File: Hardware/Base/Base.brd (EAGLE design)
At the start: 100 x 80 mm, 61 parts, among them IC1 LM2937, T1 2N3904, T10 2N3904, T2 2N3904, T3 2N3904, T4 2N3904, T5 2N3904, T6 2N3904, T7 2N3904, T8 2N3904, T9 2N3904

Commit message: Lay out components of base PCB rev0.
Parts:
- removed C1, C2: .01uF, rcl:C025-025X050
- removed IC1: LM2937, linear:TO263-3
- removed R4, R5, R6, R7: 10k, rcl:0207/7
- removed ROT-ENC: (no value), con-lstb:MA03-1
- removed TIVA1: TIVA-BOARD, tiva-board:TIVA-BOARD
- added C7, C8, C9: .01uF, rcl:C025-025X050
- added LEDGPIOC7: (no value), led:LED5MM
- added R25, R26: (no value), rcl:0207/7
- added R27, R28, R29, R30, R31, R32: 10k, rcl:0207/7
- added REG3V3: 7806T, linear:TO220H
- added ROTENC: (no value), con-lstb:MA05-1
- added SWITCH: (no value), pinhead:1X02
- added T11: 2N3904, transistor:TO92
- added TIVA: TIVA-BOARD, tiva-board:TIVA-BOARD
- X1: device con-yamaichi:USB-A003 -> con-berg:PN87520
- moved SERVO0 218.0 mm to (116.8, 76.2)
- moved LEDM1PWM3 217.2 mm to (115.6, 95.2)
- moved C4 187.6 mm to (110.5, 40.6), turned to 90 degrees
- moved T9 182.6 mm to (88.9, 90.2), turned to 180 degrees
- moved C3 179.1 mm to (120.7, 40.6), turned to 90 degrees
- moved T8 178.8 mm to (99.1, 90.2), turned to 180 degrees
- moved LEDM0PWM6 178.2 mm to (95.2, 95.2)
- moved T7 175.0 mm to (109.2, 90.2), turned to 180 degrees
- moved T6 171.2 mm to (119.4, 90.2), turned to 180 degrees
- moved LEDM0PWM0 169.4 mm to (105.4, 95.2)
- moved LCD 164.6 mm to (74.9, 6.35), turned to 180 degrees
- moved R22 163.0 mm to (99.1, 82.5), turned to 270 degrees
- moved R23 163.0 mm to (88.9, 82.5), turned to 270 degrees
- moved R20 163.0 mm to (119.4, 82.5), turned to 270 degrees
- moved R21 163.0 mm to (109.2, 82.5), turned to 270 degrees
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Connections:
- removed net N$8: C2.1, R6.1, R7.2, ROT-ENC.3
- new net GPIOC7: R26.1, R30.1, TIVA.PC7
- new net N$33: LEDGPIOC7.K, T11.1
- new net N$34: LEDGPIOC7.A, R25.1
- new net N$35: R26.2, T11.2
- new net N$36: C7.1, R27.1, R30.2, ROTENC.4
- new net N$37: C8.1, R28.1, R32.2, ROTENC.3
- new net N$38: C9.1, R29.1, R31.2, ROTENC.2
- net 3.3V: now also TIVA.3.3V; no longer TIVA1.3.3V
- net 3V3: now also LCD.3, REG3V3.3; no longer IC1.3, LCD.2
- net 5V: now also R25.2, R27.2, R28.2, R29.2, REG3V3.1, SWITCH.2, TIVA.5V; no longer IC1.1, R5.2, R7.1, TIVA1.5V, X1.1
- net GND: now also C7.2, C8.2, C9.2, LCD.2, REG3V3.2, ROTENC.1, ROTENC.5, T11.3, TIVA.GND@1, TIVA.GND@2; no longer C1.2, C2.2, IC1.2, LCD.3, ROT-ENC.2, TIVA1.GND@1, TIVA1.GND@2
- net GPIOC5: now also R31.1, TIVA.PC5; no longer R4.1, TIVA1.PC5
- net GPIOC6: now also R32.1, TIVA.PC6; no longer R6.2, TIVA1.PC6
- net GPIOE1: now also TIVA.PE1; no longer TIVA1.PE1
- net GPIOE2: now also TIVA.PE2; no longer TIVA1.PE2
- net GPIOE3: now also TIVA.PE3; no longer TIVA1.PE3
- net GPIOE5: now also TIVA.PE5; no longer TIVA1.PE5
- net M0PWM0: now also TIVA.PB6; no longer TIVA1.PB6
- net M0PWM6: now also TIVA.PC4; no longer TIVA1.PC4
- net M1PWM3: now also TIVA.PA7; no longer TIVA1.PA7
- net M1PWM4: now also TIVA.PF0; no longer TIVA1.PF0
- net M1PWM6: now also TIVA.PF2; no longer TIVA1.PF2
- net N$7: now also SWITCH.1, X1.1; no longer C1.1, R4.2, R5.1, ROT-ENC.1
- net U1RX: now also TIVA.PB0; no longer TIVA1.PB0
- net U1TX: now also TIVA.PB1; no longer TIVA1.PB1
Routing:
- added copper zone on layer 16, net GND
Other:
- board size 100 x 80 mm -> 127 x 101.6 mm

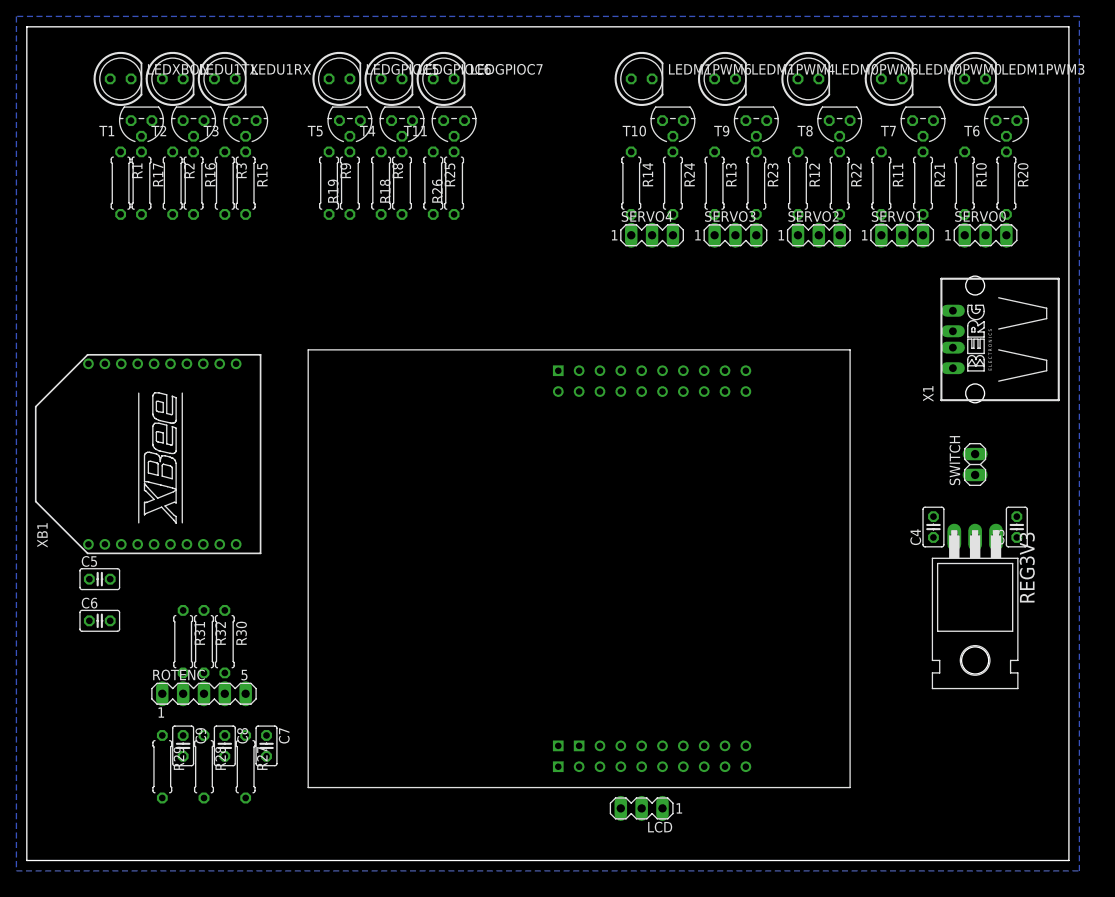
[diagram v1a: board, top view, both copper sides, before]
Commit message: Initial layout of traces.
Updated power pins on Tiva Board device.
Added most traces (except Xbee connections and a few others).
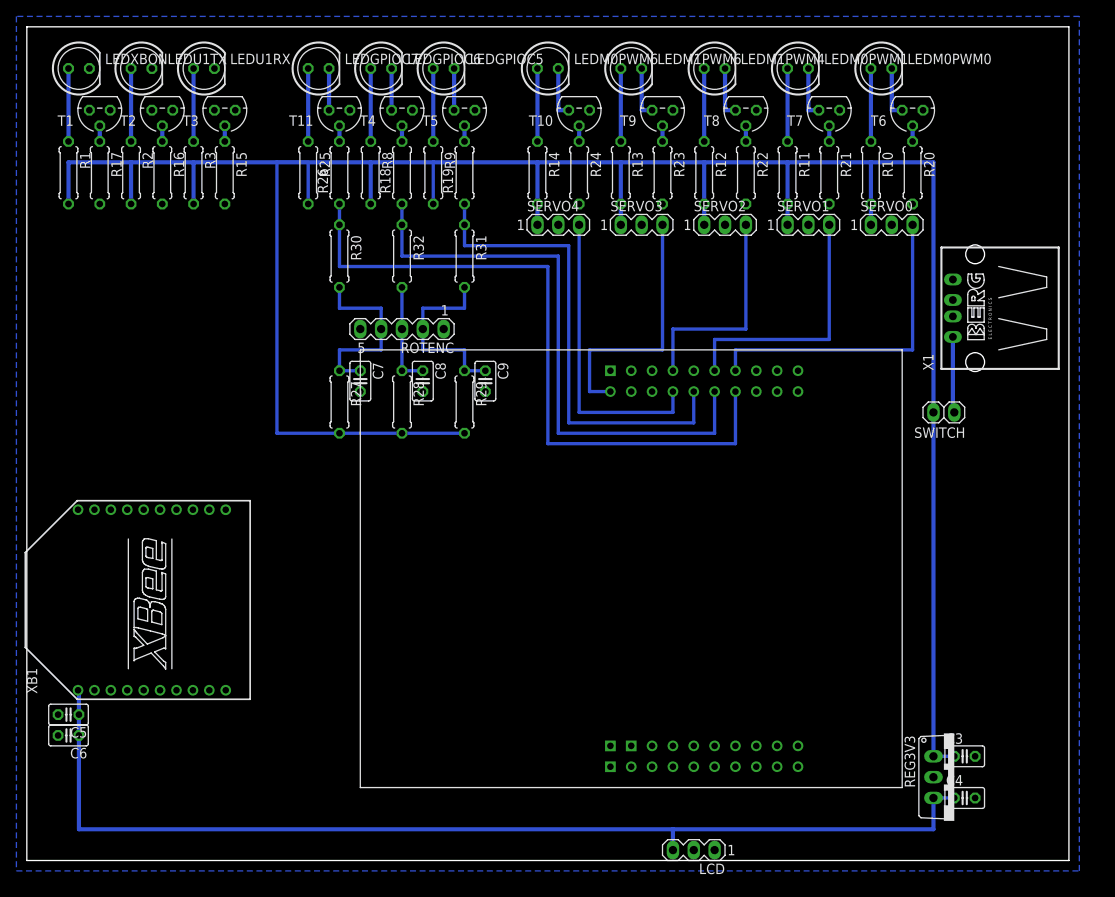
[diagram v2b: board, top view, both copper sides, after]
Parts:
- removed LEDM1PWM3: (no value), led:LED5MM
- added LEDM0PWM1: (no value), led:LED5MM
- REG3V3: value 7806T -> 7805TV; device linear:TO220H -> linear:TO220V
- moved R31 58.2 mm to (53.3, 73.7)
- moved C9 57.7 mm to (55.9, 58.4)
- moved R29 57.7 mm to (53.3, 55.9)
- moved R32 52.8 mm to (45.7, 73.7)
- moved C8 50.6 mm to (48.3, 58.4)
- moved R28 50.6 mm to (45.7, 55.9)
- moved ROTENC 50.6 mm to (45.7, 64.8), turned to 180 degrees
- moved R30 49.0 mm to (38.1, 73.7)
- moved C7 45.9 mm to (40.6, 58.4)
- moved R27 45.9 mm to (38.1, 55.9)
- moved C4 33.2 mm to (114.3, 7.62), turned to 0 degrees
- moved LEDM0PWM6 31.8 mm to (63.5, 96.5)
- moved C3 28.7 mm to (114.3, 12.7), turned to 0 degrees
- moved REG3V3 19.2 mm to (113.0, 10.2), turned to 270 degrees
- moved XB1 17.8 mm to (15.2, 31.8)
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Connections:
- removed net 3.3V: TIVA.3.3V
- removed net M1PWM3: R20.2, SERVO0.3, TIVA.PA7
- new net M0PWM1: R21.2, SERVO1.3, TIVA.PB7
- net 5V: no longer TIVA.5V
- net GND: no longer TIVA.GND@2
- net GPIOE1: no longer TIVA.PE1
- net GPIOE2: no longer TIVA.PE2
- net GPIOE3: no longer TIVA.PE3
- net GPIOE5: no longer TIVA.PE5
- net M0PWM0: now also R20.2, SERVO0.3; no longer R21.2, SERVO1.3
- net M0PWM6: now also R24.2, SERVO4.3; no longer R22.2, SERVO2.3
- net M1PWM4: now also R22.2, SERVO2.3; no longer R23.2, SERVO3.3
- net M1PWM6: now also R23.2, SERVO3.3; no longer R24.2, SERVO4.3
- net N$13: now also LEDM0PWM0.K; no longer LEDM1PWM3.K
- net N$14: now also LEDM0PWM0.A; no longer LEDM1PWM3.A
- net N$15: now also LEDM0PWM1.K; no longer LEDM0PWM0.K
- net N$16: now also LEDM0PWM1.A; no longer LEDM0PWM0.A
- net N$17: now also LEDM1PWM4.K; no longer LEDM0PWM6.K
- net N$18: now also LEDM1PWM4.A; no longer LEDM0PWM6.A
- net N$19: now also LEDM1PWM6.K; no longer LEDM1PWM4.K
- net N$20: now also LEDM1PWM6.A; no longer LEDM1PWM4.A
- net N$21: now also LEDM0PWM6.K; no longer LEDM1PWM6.K
- net N$22: now also LEDM0PWM6.A; no longer LEDM1PWM6.A
- net U1RX: no longer TIVA.PB0
- net U1TX: no longer TIVA.PB1
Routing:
- net 5V: track 0.00 -> 308.6 mm
- net 3V3: track 0.00 -> 130.1 mm
- net GPIOC7: track 0.00 -> 83.8 mm
- net GPIOC6: track 0.00 -> 71.1 mm
- net GPIOC5: track 0.00 -> 58.4 mm
- net M0PWM0: track 0.00 -> 39.4 mm
- net M0PWM6: track 0.00 -> 36.8 mm
- net M0PWM1: track 0.00 -> 31.8 mm
- net M1PWM6: track 0.00 -> 31.8 mm
- net M1PWM4: track 0.00 -> 26.7 mm
- net N$38: track 0.00 -> 22.9 mm
- net N$36: track 0.00 -> 22.9 mm
- net N$37: track 0.00 -> 12.7 mm
- net N$7: track 0.00 -> 9.37 mm
- net N$6: track 0.00 -> 8.89 mm
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
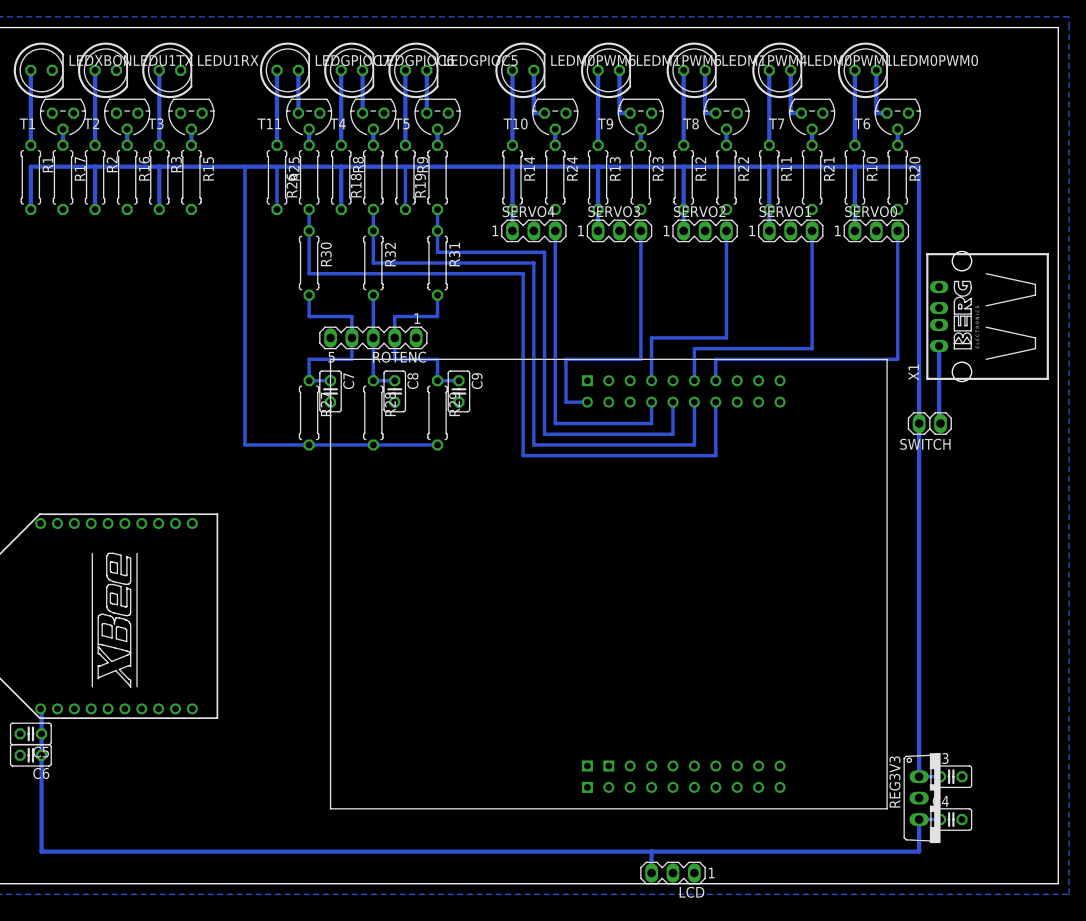
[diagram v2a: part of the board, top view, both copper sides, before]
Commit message: Add level shifter.
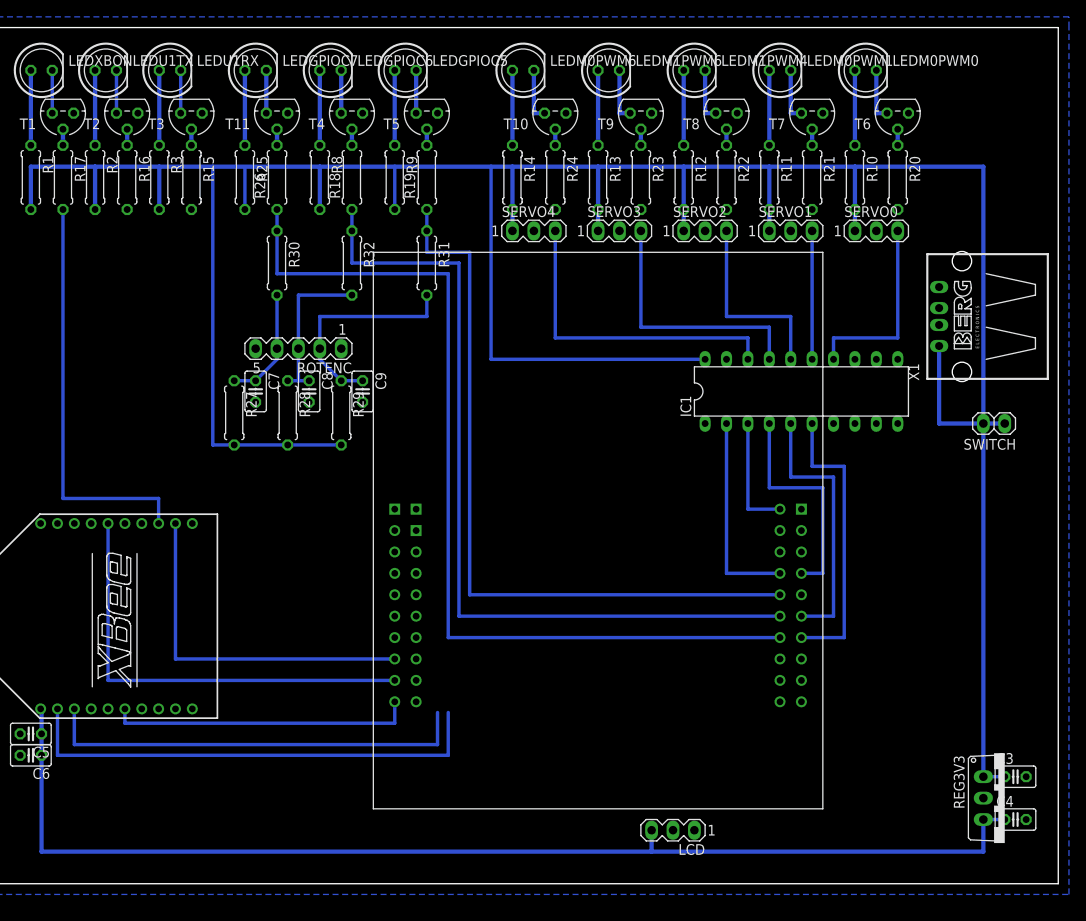
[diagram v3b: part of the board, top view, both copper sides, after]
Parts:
- added IC1: 74LS245N, 74xx-us:DIL20
- moved R29 11.4 mm to (41.9, 55.9)
- moved C9 11.4 mm to (44.5, 58.4)
- moved C8 10.2 mm to (38.1, 58.4)
- moved R28 10.2 mm to (35.6, 55.9)
- moved ROTENC 8.98 mm to (36.8, 63.5)
- moved C7 8.89 mm to (31.8, 58.4)
- moved R27 8.89 mm to (29.2, 55.9)
- moved TIVA 8.03 mm to (71.1, 41.9), turned to 0 degrees
- moved C3 7.62 mm to (121.9, 12.7)
- moved C4 7.62 mm to (121.9, 7.62)
- moved REG3V3 7.62 mm to (120.7, 10.2)
- moved SWITCH 7.62 mm to (119.4, 54.6)
- moved LCD 5.08 mm to (81.3, 6.35)
- moved LEDGPIOC7 3.81 mm to (31.8, 96.5)
- moved R26 3.81 mm to (34.3, 83.8)
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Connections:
- removed net GPIOE1: XB1.6
- removed net GPIOE2: XB1.12
- removed net GPIOE3: XB1.16
- new net CTS: TIVA.PA5, XB1.12
- new net N$39: IC1.4, TIVA.PF0
- new net N$40: IC1.3, TIVA.PF2
- new net N$41: IC1.5, TIVA.PB7
- new net N$42: IC1.6, TIVA.PB6
- new net N$8: IC1.2, TIVA.PC4
- new net RSSI: TIVA.PA7, XB1.6
- new net RTS: TIVA.PA6, XB1.16
- net 5V: now also IC1.20
- net GND: now also IC1.10
- net M0PWM0: now also IC1.14; no longer TIVA.PB6
- net M0PWM1: now also IC1.15; no longer TIVA.PB7
- net M0PWM6: now also IC1.18; no longer TIVA.PC4
- net M1PWM4: now also IC1.16; no longer TIVA.PF0
- net M1PWM6: now also IC1.17; no longer TIVA.PF2
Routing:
- net U1RX: track 0.00 -> 57.0 mm
- net RTS: track 0.00 -> 52.6 mm
- net U1TX: track 0.00 -> 51.2 mm
- net XBON: track 0.00 -> 48.6 mm
- net 5V: track 308.6 -> 356.9 mm
- net CTS: track 0.00 -> 42.1 mm
- net RSSI: track 0.00 -> 36.3 mm
- net N$42: track 0.00 -> 34.3 mm
- net N$41: track 0.00 -> 31.8 mm
- net GPIOC5: track 58.4 -> 87.6 mm
- net GPIOC6: track 71.1 -> 99.1 mm
- net N$39: track 0.00 -> 26.7 mm
- net GPIOC7: track 83.8 -> 110.5 mm
- net N$8: track 0.00 -> 24.1 mm
- net M0PWM1: track 31.8 -> 15.2 mm
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
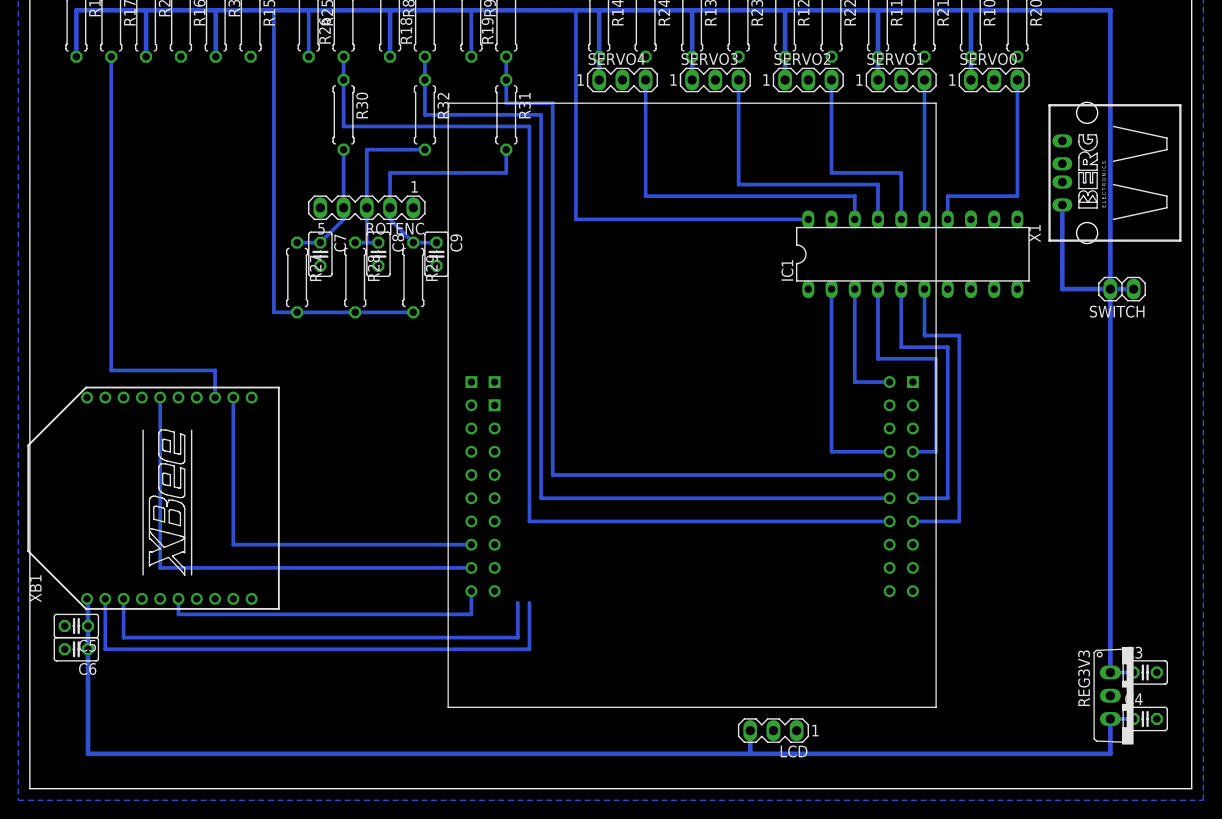
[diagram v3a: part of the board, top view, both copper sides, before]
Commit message: Begin Xbee connections.
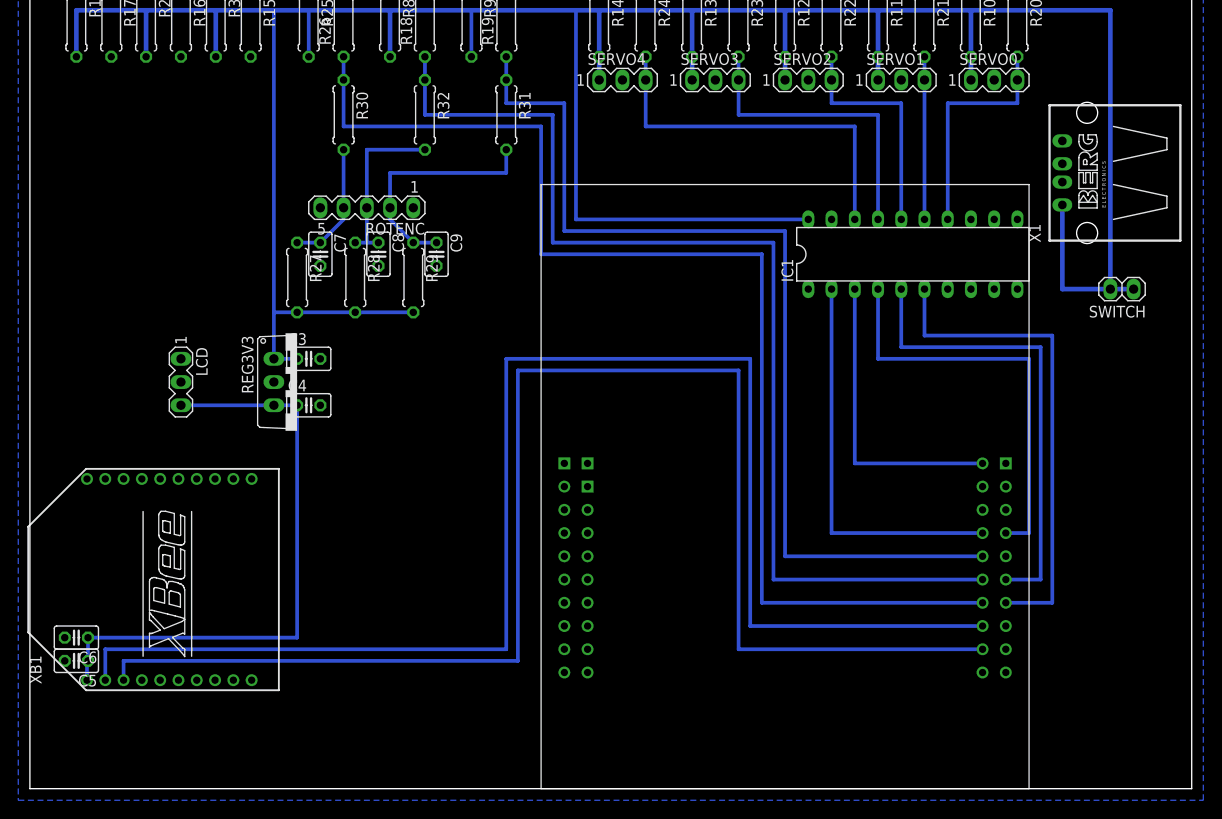
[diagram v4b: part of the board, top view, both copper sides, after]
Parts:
- moved C3 97.7 mm to (30.5, 47.0)
- moved C4 97.7 mm to (30.5, 41.9)
- moved REG3V3 97.7 mm to (29.2, 44.5)
- moved LCD 75.1 mm to (16.5, 44.5), turned to 270 degrees
- moved TIVA 13.5 mm to (81.3, 33.0)
- moved XB1 8.89 mm to (15.2, 22.9)
- moved C5 3.81 mm to (5.08, 14.0)
- moved C6 1.27 mm to (5.08, 16.5)
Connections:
- net U1RX: now also TIVA.PD6
- net U1TX: now also TIVA.PD7
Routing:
- net U1TX: track 51.2 -> 158.2 mm
- net U1RX: track 57.0 -> 160.2 mm
- net 3V3: track 137.7 -> 65.8 mm
- net RTS: track 52.6 -> 0.00 mm
- net XBON: track 48.6 -> 0.00 mm
- net CTS: track 42.1 -> 0.00 mm
- net 5V: track 356.9 -> 320.0 mm
- net RSSI: track 36.3 -> 0.00 mm
- net N$42: track 34.3 -> 53.3 mm
- net N$8: track 24.1 -> 43.2 mm
- net N$40: track 14.0 -> 33.0 mm
- net GPIOC6: track 99.1 -> 118.1 mm
- net GPIOC5: track 87.6 -> 106.7 mm
- net N$41: track 31.8 -> 50.8 mm
- net N$39: track 26.7 -> 45.7 mm
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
